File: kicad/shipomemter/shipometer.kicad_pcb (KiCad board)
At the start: 2 copper layers, 65 x 56.5 mm, 36 parts, among them J101 Raspberry_Pi_40, J102 Conn_01x03, J104 ICM20948, J105 BME280, J106 ZED-F9R, U102 74LS138, U1201 LPC2103, U401 TCR2EF 3.3V, U501 TCR2EF 1.8V, Y1201 12MHz

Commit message: Imported BME280 stamp
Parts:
- added C506: 100nF, Capacitor_SMD:C_0603_1608Metric, F.Cu at (151.4, 110.5)
- added C508: 100nF, Capacitor_SMD:C_0603_1608Metric, F.Cu at (153.4, 110.5)
- added G1: github.com/kwan3217, KwanSystems:KWAN_CIRCLE, B.Cu at (152.4, 114.3)
- added G2: Designed with, KwanSystems:Symbol_KiCAD-Logo_CopperAndSilkScreenTop_small, B.Cu at (155.7, 120.4)
- added G3: OSHW, KwanSystems:OSHW-Symbol_4x3.6mm_SolderMask, B.Cu at (148.1, 119.9)
- added J101: ~, KwanSystems:Stamp, F.Cu at (152.4, 114.3)
- added U1: BME280, Package_LGA:Bosch_LGA-8_2.5x2.5mm_P0.65mm_ClockwisePinNumbering, F.Cu at (152.4, 114.3)
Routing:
- net (no net): track 0.00 -> 82.2 mm, vias 0 -> 3
- net +3V3: track 137.3 -> 172.8 mm
- net GND: vias 0 -> 3
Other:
- board text added: "2023-04-01"
- board text added: "23.04"

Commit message: Pulled in ICM20948
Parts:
- added C302: 100nF, Capacitor_SMD:C_0603_1608Metric, F.Cu at (167.4, 109.2)
- added C308: 1uF, Capacitor_SMD:C_0603_1608Metric, F.Cu at (170.9, 120.7)
- added C310: 100nF, Capacitor_SMD:C_0603_1608Metric, F.Cu at (174.5, 120.7)
- added C313: 100nF, Capacitor_SMD:C_0603_1608Metric, F.Cu at (177.3, 116.8)
- added C319: 100nF, Capacitor_SMD:C_0603_1608Metric, F.Cu at (178.1, 109.2)
- added G301: KwanSystems, KwanSystems:KWAN_CIRCLE, B.Cu at (172.7, 114.3)
- added G302: Designed with, KwanSystems:Symbol_KiCAD-Logo_CopperAndSilkScreenTop_small, B.Cu at (176.0, 120.4)
- added G303: OSHW, KwanSystems:OSHW-Symbol_4x3.6mm_SolderMask, B.Cu at (168.1, 119.6)
- added J301: ~, KwanSystems:Stamp, F.Cu at (172.7, 114.3)
- added U301: ICM-20948, Sensor_Motion:InvenSense_QFN-24_3x3mm_P0.4mm, F.Cu at (172.7, 116.8)
- added U302: TXS0108EPW, Package_SO:TSSOP-20_4.4x6.5mm_P0.65mm, F.Cu at (172.7, 110.5)
- G201: renamed from G1; value github.com/kwan3217 -> KwanSystems
- renumbered C506 to C206, C508 to C208, G2 to G202, G3 to G203, J101 to J201, U1 to U201
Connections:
- J104 pad 8: unconnected-(J104-AD0-Pad8) -> /DRDY_6D
- J104 pad 9: /DRDY_6D -> unconnected-(J104-AD0-Pad9)
- J105 pad 1: +3V3 -> unconnected-(J105-Pad1)
- J201 pad 1: +3V3 -> unconnected-(J201-1V8-Pad1)
- J201 pad 10: (no net) -> /Pressure/MOSI
- J201 pad 11: (no net) -> /Pressure/SCK
- J201 pad 2: (no net) -> /Pressure/MISO
- J201 pad 3: (no net) -> /Pressure/MOSI
- J201 pad 4: (no net) -> /Pressure/SCK
- J201 pad 5: (no net) -> /Pressure/~{CS}
- J201 pad 8: (no net) -> unconnected-(J201-Pad8)
- J201 pad 9: (no net) -> /Pressure/MISO
- U201 pad 2: (no net) -> /Pressure/~{CS}
- U201 pad 3: (no net) -> /Pressure/MOSI
- U201 pad 4: (no net) -> /Pressure/SCK
- U201 pad 5: (no net) -> /Pressure/MISO
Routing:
- net (no net): track 82.2 -> 0.00 mm, vias 3 -> 0
- net /Pressure/MOSI: track 0.00 -> 30.4 mm, vias 0 -> 1
- net +1V8: track 34.6 -> 64.7 mm, vias 3 -> 5
- net /IMU/MISO_3V3: track 0.00 -> 23.8 mm, vias 0 -> 3
- net /Pressure/SCK: track 0.00 -> 21.1 mm, vias 0 -> 1
- net /IMU/MOSI_3V3: track 0.00 -> 19.9 mm, vias 0 -> 1
- net /IMU/MISO_1V8: track 0.00 -> 19.3 mm, vias 0 -> 2
- net /IMU/SCK_3V3: track 0.00 -> 19.2 mm, vias 0 -> 1
- net /Pressure/MISO: track 0.00 -> 18.7 mm, vias 0 -> 1
- net /IMU/INT1_1V8: track 0.00 -> 16.5 mm, vias 0 -> 2
- net /IMU/~{CS}_3V3: track 0.00 -> 13.8 mm, vias 0 -> 1
- net /Pressure/~{CS}: track 0.00 -> 12.0 mm
- net /IMU/INT1_3V3: track 0.00 -> 11.6 mm
- net /IMU/MOSI_1V8: track 0.00 -> 9.15 mm, vias 0 -> 2
- net /IMU/SCK_1V8: track 0.00 -> 7.82 mm, vias 0 -> 2
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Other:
- board text added: "ICM20948 Stamp 01 Apr 2023"
- board text removed: "23.04"

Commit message: As ordered on 03 Apr 2023. Some but not all numbers-on-hand have been updated.
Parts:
- added C116: 1uF, Capacitor_SMD:C_0603_1608Metric, F.Cu at (181.0, 75.7)
- added C801: 1uF, Capacitor_SMD:C_0603_1608Metric, F.Cu at (199.9, 114.3)
- added C805: 1uF, Capacitor_SMD:C_0603_1608Metric, F.Cu at (193.8, 114.3)
- added G701: github.com/kwan3217, KwanSystems:KWAN_CIRCLE, B.Cu at (196.8, 114.3)
- added G702: Designed with, KwanSystems:Symbol_KiCAD-Logo_CopperAndSilkScreenTop_small, F.Cu at (199.0, 120.3)
- added G703: OSHW, KwanSystems:OSHW-Symbol_4x3.6mm_SolderMask, F.Cu at (193.2, 119.6)
- added J701: Conn_01x06_Pin, Connector_PinHeader_2.54mm:PinHeader_1x06_P2.54mm_Vertical, F.Cu at (184.2, 108.0)
- added J702: Conn_01x06_Pin, Connector_PinHeader_2.54mm:PinHeader_1x06_P2.54mm_Vertical, F.Cu at (189.2, 108.0)
- added J703: Conn_01x06_Pin, Connector_PinHeader_2.54mm:PinHeader_1x06_P2.54mm_Vertical, F.Cu at (208.9, 120.7)
- added J704: Conn_01x06_Pin, Connector_PinHeader_2.54mm:PinHeader_1x06_P2.54mm_Vertical, F.Cu at (203.8, 120.7)
- added U801: TCR2EF 1.8V, Package_TO_SOT_SMD:SOT-23-5, F.Cu at (196.8, 114.3)
- C206, C208: value 100nF -> 1uF
- C308: value 1uF -> 100nF
- C605: renamed from C1205; value 100nF -> 1uF
- C617: renamed from C1217; value 100nF -> 1uF
- C640: renamed from C1240; value 100nF -> 1uF
- G201, G301: value KwanSystems -> github.com/kwan3217
- renumbered C1211 to C611, C1212 to C612, U1201 to U601, Y1201 to Y601
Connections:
- C206 pad 1: +3V3 -> /Pressure/Q_3V3
- C206 pad 2: GND -> /Pressure/Q_GND
- C208 pad 1: +3V3 -> /Pressure/Q_3V3
- C208 pad 2: GND -> /Pressure/Q_GND
- C302 pad 1: +1V8 -> /IMU/Q_1V8
- C302 pad 2: GND -> /IMU/Q_GND
- C308 pad 1: +1V8 -> /IMU/Q_1V8
- C308 pad 2: GND -> /IMU/Q_GND
- C310 pad 2: GND -> /IMU/Q_GND
- C313 pad 1: +1V8 -> /IMU/Q_1V8
- C313 pad 2: GND -> /IMU/Q_GND
- C319 pad 1: +3V3 -> /IMU/Q_3V3
- C319 pad 2: GND -> /IMU/Q_GND
- J201 pad 12: +3V3 -> /Pressure/Q_3V3
- J201 pad 6: GND -> /Pressure/Q_GND
- J201 pad 7: GND -> /Pressure/Q_GND
- J301 pad 1: +1V8 -> /IMU/Q_1V8
- J301 pad 12: +3V3 -> /IMU/Q_3V3
- J301 pad 6: GND -> /IMU/Q_GND
- J301 pad 7: GND -> /IMU/Q_GND
- U201 pad 1: GND -> /Pressure/Q_GND
- U201 pad 6: +3V3 -> /Pressure/Q_3V3
- U201 pad 7: GND -> /Pressure/Q_GND
- U201 pad 8: +3V3 -> /Pressure/Q_3V3
- U301 pad 13: +1V8 -> /IMU/Q_1V8
- U301 pad 18: GND -> /IMU/Q_GND
- U301 pad 20: GND -> /IMU/Q_GND
- U301 pad 8: +1V8 -> /IMU/Q_1V8
- U302 pad 10: +1V8 -> /IMU/Q_1V8
- U302 pad 11: GND -> /IMU/Q_GND
- U302 pad 19: +3V3 -> /IMU/Q_3V3
- U302 pad 2: +1V8 -> /IMU/Q_1V8
- U302 pad 6: GND -> /IMU/Q_GND
- U302 pad 8: GND -> /IMU/Q_GND
- U302 pad 9: GND -> /IMU/Q_GND
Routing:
- net +3V3: track 166.4 -> 133.9 mm
- net /IMU/Q_1V8: track 0.00 -> 30.1 mm, vias 0 -> 2
- net +1V8: track 64.7 -> 34.6 mm, vias 5 -> 3
- net /Pressure/Q_3V3: track 0.00 -> 23.2 mm
- net /Stamp Tester/Q_3V3: track 0.00 -> 22.3 mm
- net /Stamp Tester/Q_1V8: track 0.00 -> 16.1 mm
- net /IMU/Q_3V3: track 0.00 -> 5.86 mm
- net /~{DRDY}_MAG_ECHO: track 72.3 -> 67.1 mm
- net /Stamp Tester/Q_~{CS}: track 0.00 -> 5.08 mm
- net /Stamp Tester/Q_SDA: track 0.00 -> 5.08 mm
- net /Stamp Tester/Q_SCL: track 0.00 -> 5.08 mm
- net /Stamp Tester/Q_SCK: track 0.00 -> 5.08 mm
- net /Stamp Tester/Q_MOSI: track 0.00 -> 5.08 mm
- net /Stamp Tester/Q_MISO: track 0.00 -> 5.08 mm
- net /Stamp Tester/Q_DRDY: track 0.00 -> 5.08 mm
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- added copper zone on B.Cu, net /IMU/Q_GND
- added copper zone on F.Cu, net /IMU/Q_GND
- added copper zone on B.Cu, net /Pressure/Q_GND
- added copper zone on F.Cu, net /Pressure/Q_GND
- added copper zone on B.Cu, net /Stamp Tester/Q_GND
- added copper zone on F.Cu, net /Stamp Tester/Q_GND
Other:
- board size 65 x 56.5 mm -> 65 x 75.1 mm
- board text added: "03 Apr 2023"
- board text added: "1V8"
- board text added: "3V3"
- board text added: "AD0"
- board text added: "BME280 Stamp 03 Apr 2023"
- board text added: "GND"
- board text added: "ICM20948 Stamp 03 Apr 2023"
- board text added: "MISO"
- board text added: "MOSI"
- board text added: "RDY"
- board text added: "SCK"
- board text added: "SCL"
- board text added: "SDA"
- board text added: "Stamp Tester 23.04"
- board text added: "~{CS}"
- board text removed: "01 Apr 2023"
- board text removed: "2023-04-01"
- board text removed: "ICM20948 Stamp 01 Apr 2023"

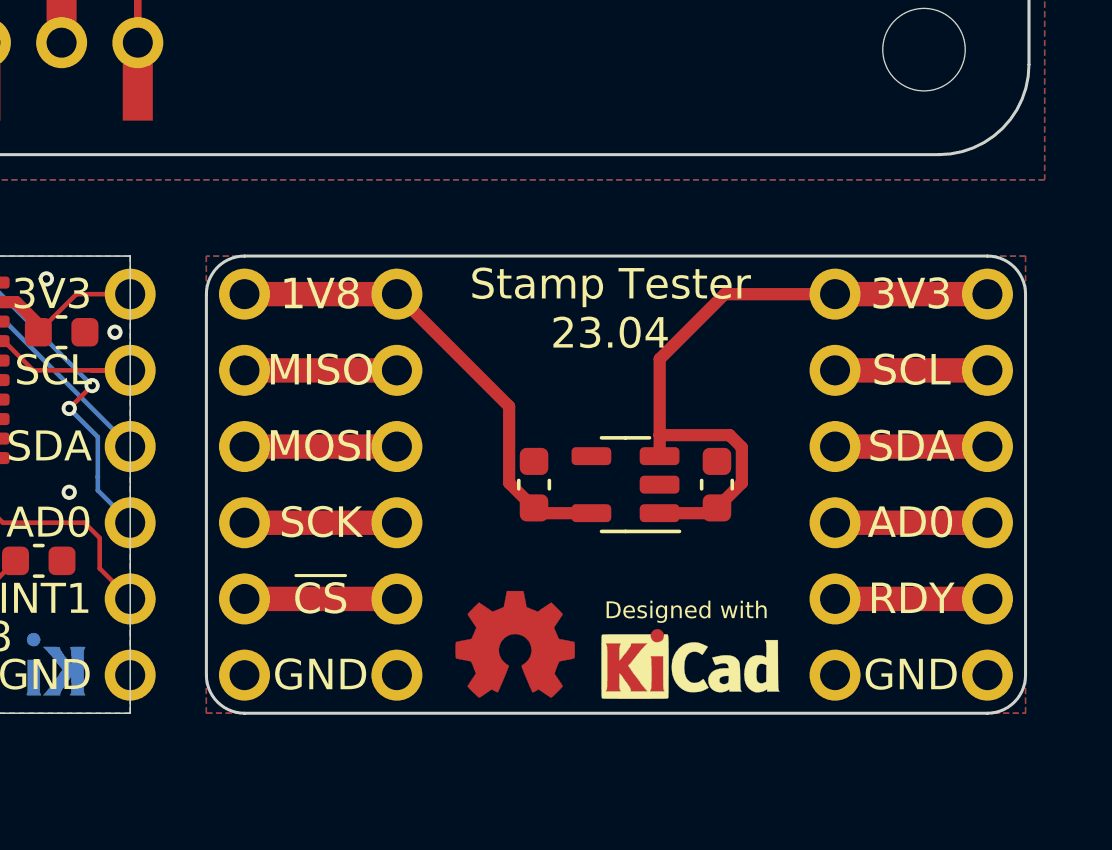
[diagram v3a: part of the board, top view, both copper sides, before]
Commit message: Updated numbers on hand and numbers in cart
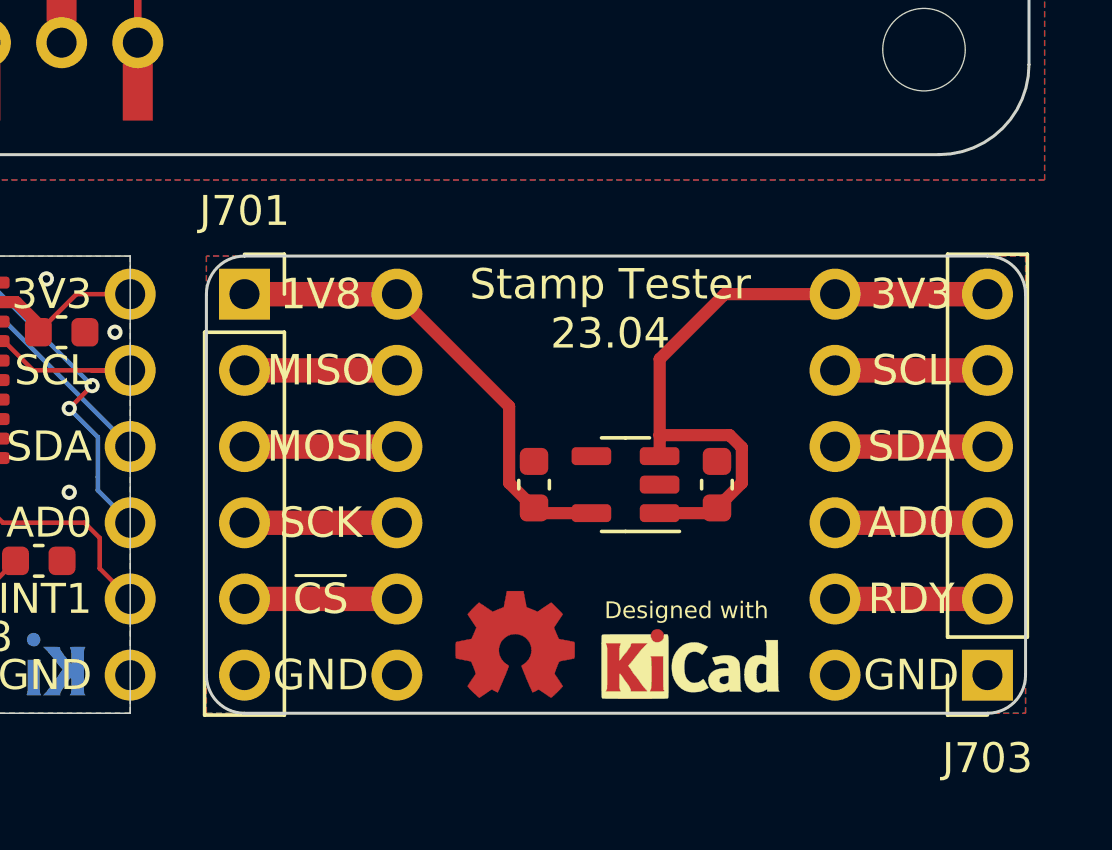
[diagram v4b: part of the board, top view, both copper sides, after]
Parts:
- J701, J703: footprint Connector_PinHeader_2.54mm:PinHeader_1x06_P2.54mm_Vertical -> Connector_PinSocket_2.54mm:PinSocket_1x06_P2.54mm_Vertical

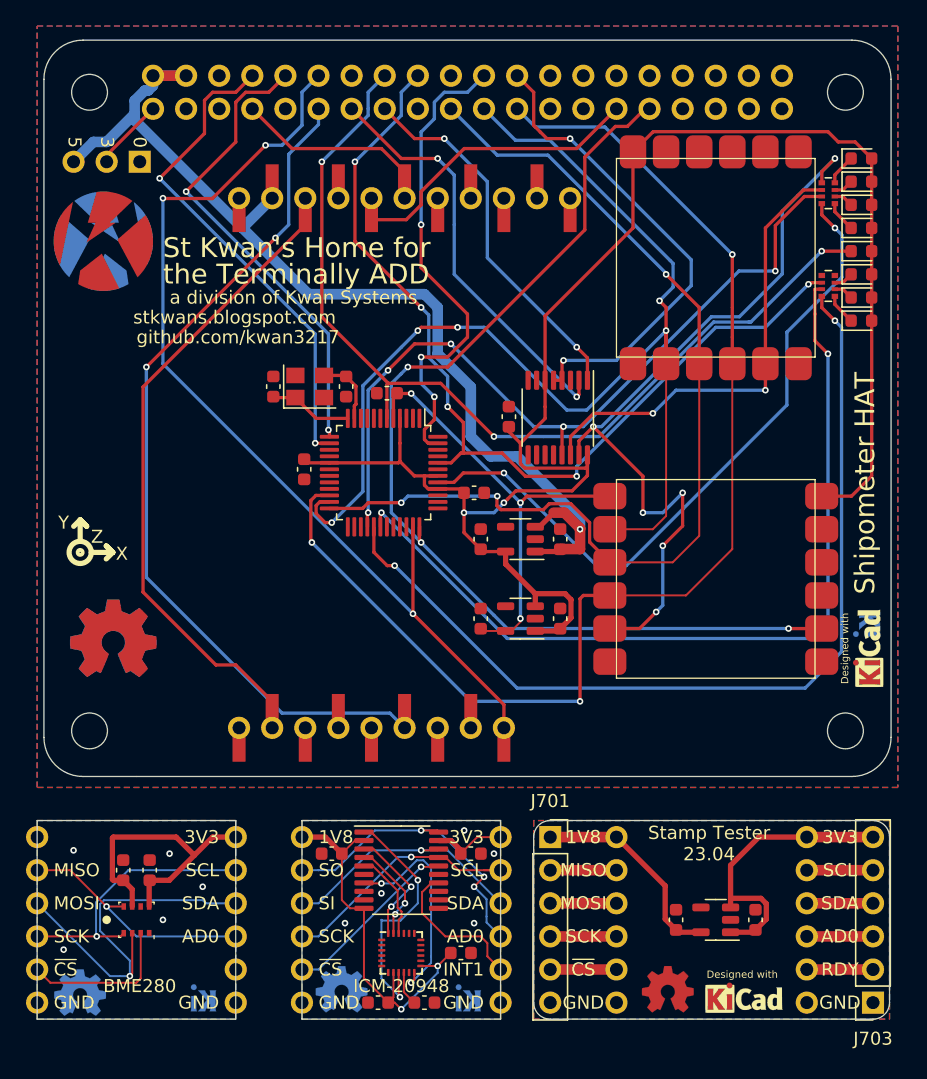
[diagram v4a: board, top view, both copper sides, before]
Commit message: Updated stuff that was needed to make Shipometer 23.04 case
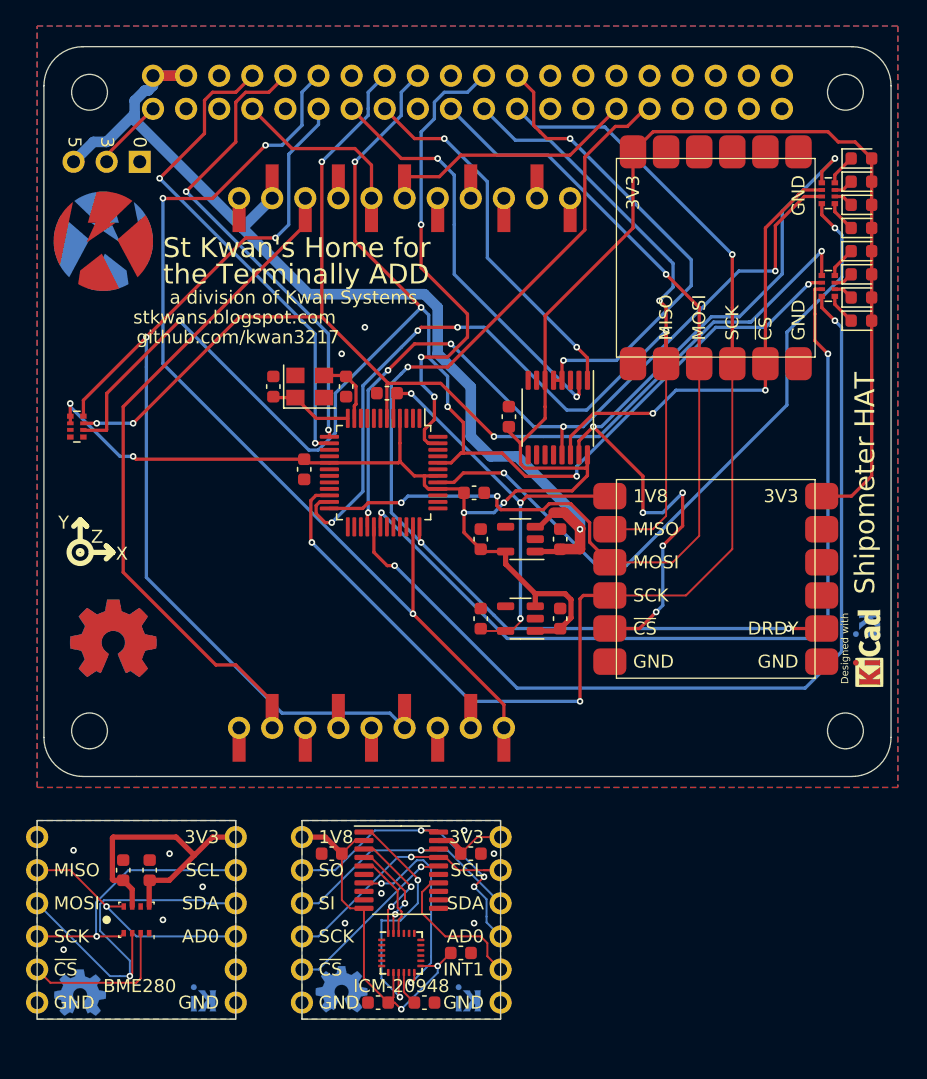
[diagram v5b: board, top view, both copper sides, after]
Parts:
- removed C801, C805: 1uF, Capacitor_SMD:C_0603_1608Metric
- removed G701: github.com/kwan3217, KwanSystems:KWAN_CIRCLE
- removed G702: Designed with, KwanSystems:Symbol_KiCAD-Logo_CopperAndSilkScreenTop_small
- removed G703: OSHW, KwanSystems:OSHW-Symbol_4x3.6mm_SolderMask
- removed J701, J703: Conn_01x06_Pin, Connector_PinSocket_2.54mm:PinSocket_1x06_P2.54mm_Vertical
- removed J702, J704: Conn_01x06_Pin, Connector_PinHeader_2.54mm:PinHeader_1x06_P2.54mm_Vertical
- removed U801: TCR2EF 1.8V, Package_TO_SOT_SMD:SOT-23-5
- added R103: 10k, KwanSystems:R_Array_Convex_4x0402, F.Cu at (147.8, 76.5)
- J101: footprint KwanSystems:PiHAT -> KwanSystems:PiHAT_NoSlot_Narrow
- R101, R102: value 68 -> 330
- U601: value LPC2103 -> LPC210x
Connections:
- D106 pad 1: /LPC_~{RESET} -> /LPC_RESET-
- J101 pad 29: /GPS_RX -> /GPS_TX
- J101 pad 7: /GPS_TX -> /GPS_RX
- R102 pad 1: unconnected-(R102A-4-Pad1) -> /LPC_~{RESET}
- R102 pad 8: unconnected-(R102A-5-Pad8) -> /LPC_RESET-
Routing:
- net /LPC_~{BOOTSTRAP}: track 71.5 -> 113.0 mm, vias 5 -> 6
- net /Stamp Tester/Q_3V3: track 22.3 -> 0.00 mm
- net +3V3: track 133.9 -> 155.3 mm, vias 2 -> 4
- net /LPC_~{RESET}: track 73.5 -> 94.8 mm, vias 3 -> 5
- net /Stamp Tester/Q_1V8: track 16.1 -> 0.00 mm
- net /GPS_~{RESET}: track 66.0 -> 76.0 mm
- net /GPS_RX: track 22.9 -> 13.5 mm
- net /Stamp Tester/Q_~{CS}: track 5.08 -> 0.00 mm
- net /Stamp Tester/Q_SDA: track 5.08 -> 0.00 mm
- net /Stamp Tester/Q_SCL: track 5.08 -> 0.00 mm
- net /Stamp Tester/Q_SCK: track 5.08 -> 0.00 mm
- net /Stamp Tester/Q_MOSI: track 5.08 -> 0.00 mm
- net /Stamp Tester/Q_MISO: track 5.08 -> 0.00 mm
- net /Stamp Tester/Q_DRDY: track 5.08 -> 0.00 mm
- net /Stamp Tester/Q_AD0: track 5.08 -> 0.00 mm
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- removed copper zone on B.Cu, net /Stamp Tester/Q_GND
- removed copper zone on F.Cu, net /Stamp Tester/Q_GND
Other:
- board size 65 x 75.1 mm -> 65 x 56 mm
- board text added: "05 May 2023"
- board text added: "Version 23.05"
- board text removed: "03 Apr 2023"
- board text removed: "1V8"
- board text removed: "3V3"
- board text removed: "AD0"
- board text removed: "GND"
- board text removed: "MISO"
- board text removed: "MOSI"
- board text removed: "RDY"
- board text removed: "SCK"
- board text removed: "SCL"
- board text removed: "SDA"
- board text removed: "Stamp Tester 23.04"
- board text removed: "Version 23.04 No Shoe"
- board text removed: "~{CS}"
